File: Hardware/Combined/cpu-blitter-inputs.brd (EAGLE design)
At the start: 177.8 x 152.4 mm, 146 parts, among them IC1 74S08N, IC12 74S08N, IC16 7404N, IC18 7432N, IC20 7430N, IC21 7400N, IC3 74HC573N, IC31 7400N, IC32 7432N, IC4 7404N, IC5 7400N, IC53 7404N, IC54 74LS07N, IC7 74S08N, IC9 74LS74N, J2 TX25-40P-6ST-H1E, U1 W65C02SP, U2 VIA

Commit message: add SMD oscillator to library and fix GRAM power connections
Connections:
- removed net VDD: U$4.32
- removed net VSS: U$4.16
- net GND: now also U$4.16
- net VCC: now also U$4.32
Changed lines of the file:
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@@
 <contactref element="IC3" pad="20"/>
 <contactref element="U$5" pad="28"/>
+<contactref element="U$4" pad="32"/>
 </signal>
 <signal name="GND">
@@
 <contactref element="IC3" pad="1"/>
 <contactref element="U$5" pad="14"/>
+<contactref element="U$4" pad="16"/>
 </signal>
 <signal name="N$1">
@@
 <wire x1="149.86" y1="-17.78" x2="145.0975" y2="-13.0175" width="0.1524" layer="1"/>
 </signal>
-<signal name="VSS">
-<contactref element="U$4" pad="16"/>
-</signal>
-<signal name="VDD">
-<contactref element="U$4" pad="32"/>
-</signal>
 <signal name="AUD_RESET">

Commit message: fix ACP control lines (in schematic)
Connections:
- removed net AUD_SQ1_N: WR_REG_DECODE.15
- removed net AUD_SQ1_X: WR_REG_DECODE.14
- removed net AUD_WAVE_X: WR_REG_DECODE.9
- net !AUD_NMI: now also WR_REG_DECODE.14
- net AUD_RESET: now also WR_REG_DECODE.15
- net AUD_SAMP_RATE_SEL: now also WR_REG_DECODE.9
- net GND: no longer VIAPORT.1
- net VCC: now also VIAPORT.1

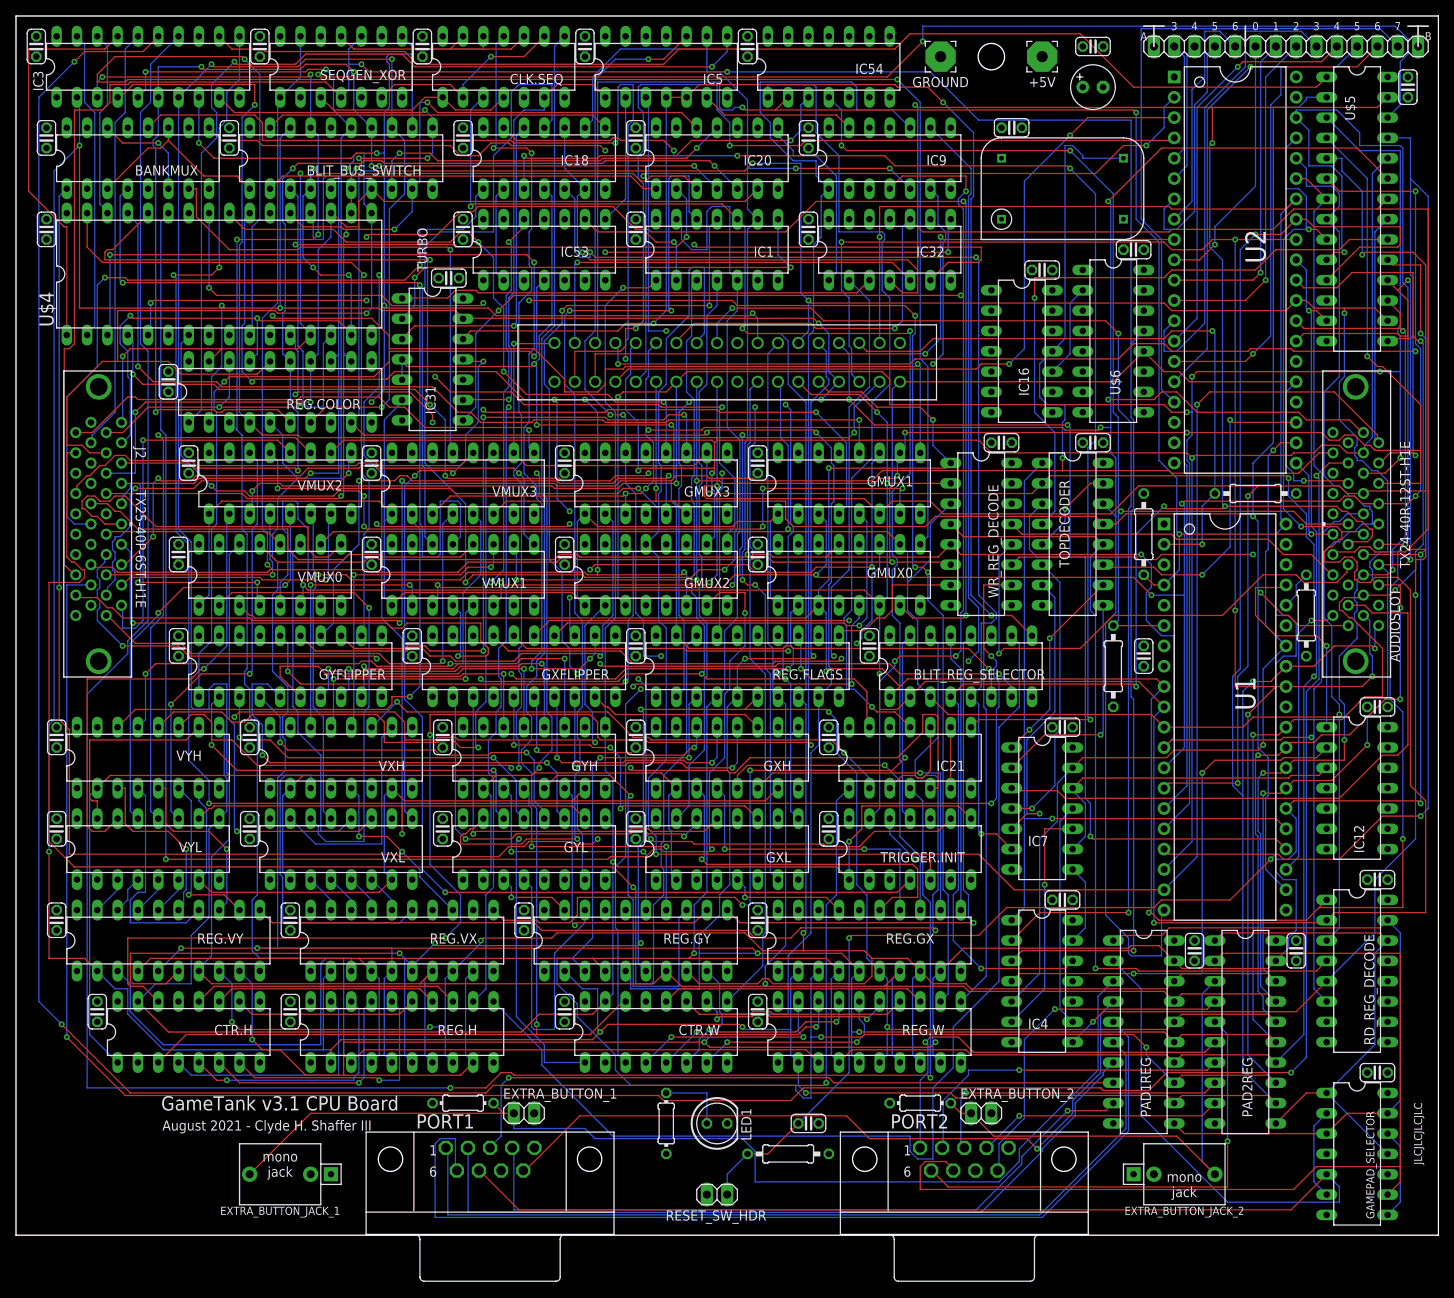
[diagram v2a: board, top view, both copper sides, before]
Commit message: Replace MUX for readregs with spare gates
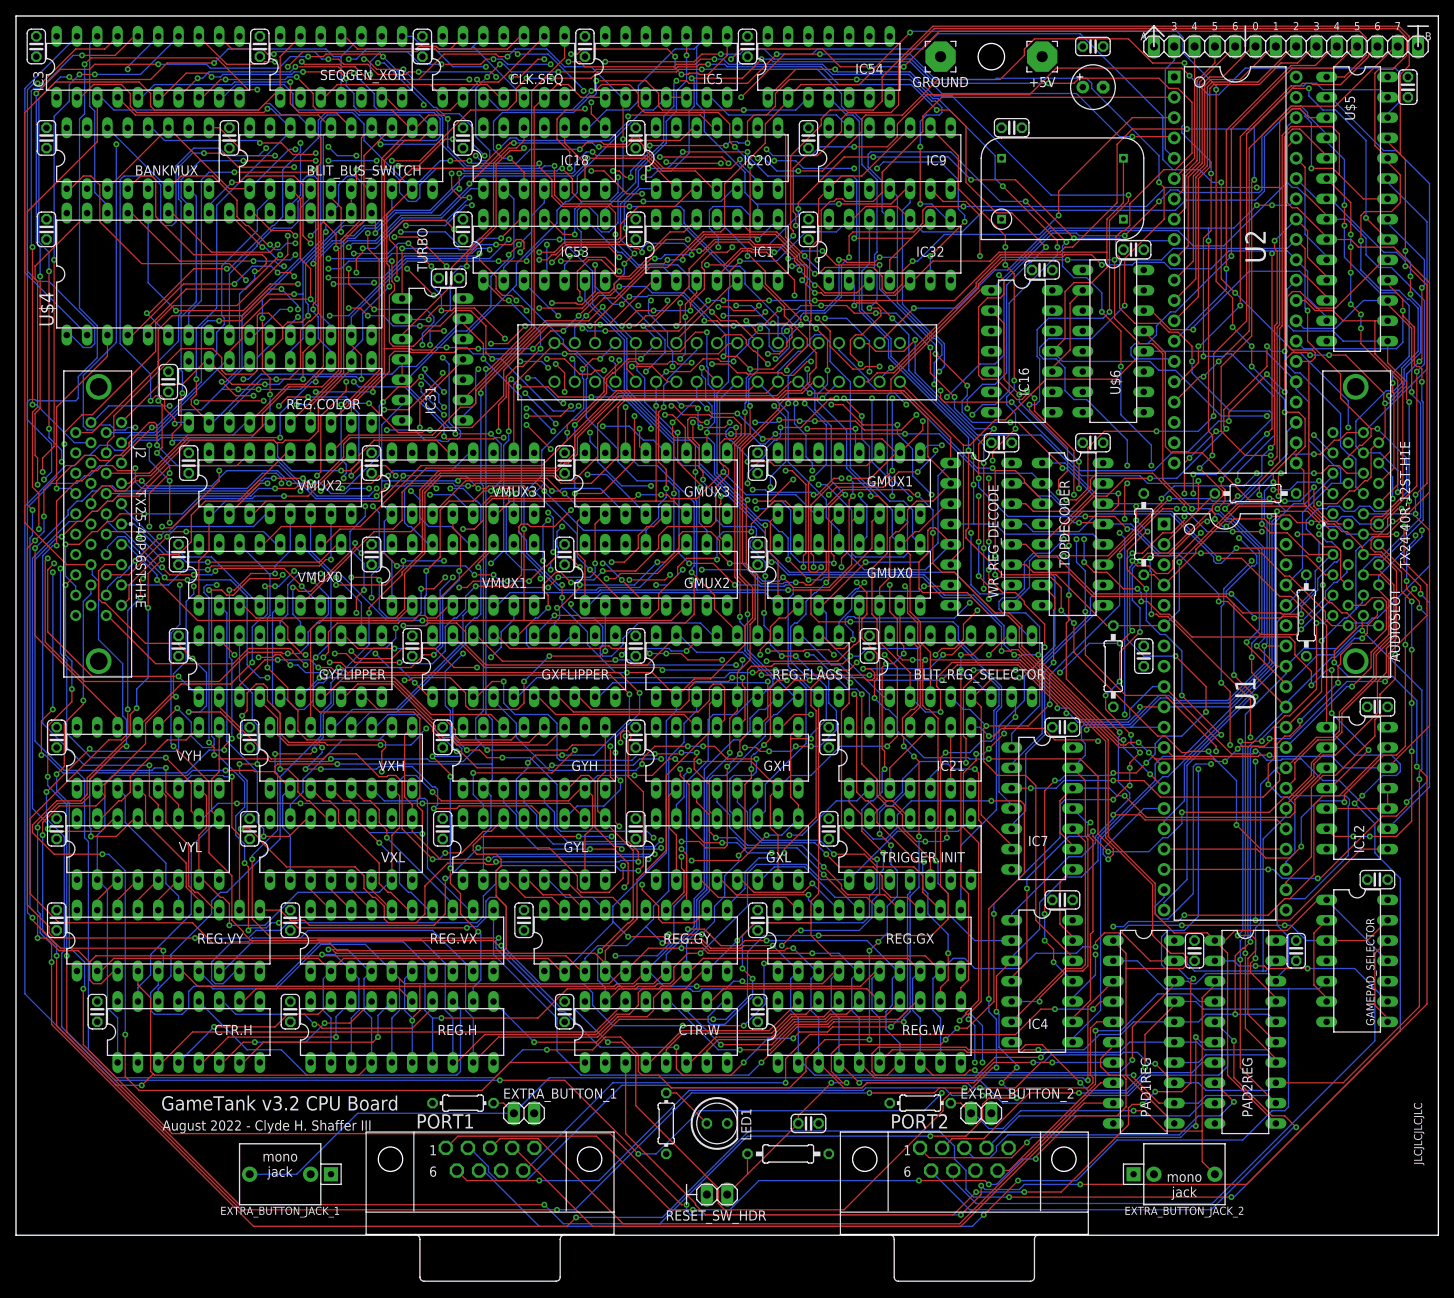
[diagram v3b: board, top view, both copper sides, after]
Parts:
- removed C37: (no value), rcl:C025-024X044
- removed RD_REG_DECODE: 74LS138N, 74xx-us:DIL16
- moved C36 24.1 mm to (170.2, 19.1)
- moved GAMEPAD_SELECTOR 24.1 mm to (167.6, 8.89)
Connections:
- removed net N$91: RD_REG_DECODE.13
- removed net N$92: RD_REG_DECODE.12
- removed net N$93: RD_REG_DECODE.11
- removed net N$95: RD_REG_DECODE.10
- removed net N$97: RD_REG_DECODE.9
- removed net N$99: RD_REG_DECODE.7
- new net N$129: IC12.6, IC53.5
- new net N$149: IC12.13, IC4.10
- new net N$152: IC32.11, IC4.11
- new net N$153: IC12.10, IC12.11, IC12.5
- new net N$154: IC12.4, IC16.2
- new net N$34: IC12.8, IC53.11
- net !GAMEPAD1R: now also IC53.6; no longer RD_REG_DECODE.15
- net !GAMEPAD2R: now also IC53.10; no longer RD_REG_DECODE.14
- net !RE2: now also IC32.13; no longer RD_REG_DECODE.5
- net !REGSSEL: now also IC32.12; no longer RD_REG_DECODE.4
- net A0: now also IC12.9, IC16.1; no longer RD_REG_DECODE.1
- net A1: no longer RD_REG_DECODE.2
- net A2: no longer RD_REG_DECODE.3
- net A3: now also IC12.12; no longer RD_REG_DECODE.6
- net GND: no longer C37.2, RD_REG_DECODE.8
- net VCC: no longer C37.1, RD_REG_DECODE.16
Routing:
- net N$34: track 0.00 -> 248.6 mm, vias 0 -> 16
- net CLK3_5: track 318.9 -> 549.7 mm, vias 4 -> 8
- net N$129: track 0.00 -> 227.2 mm, vias 0 -> 14
- net N$125: track 104.3 -> 293.4 mm, vias 2 -> 15
- net N$152: track 0.00 -> 166.8 mm, vias 0 -> 15
- net N$2: track 157.3 -> 299.4 mm, vias 3 -> 13
- net !GAMEPAD2R: track 63.3 -> 194.3 mm, vias 0 -> 3
- net D0: track 709.6 -> 586.2 mm, vias 13 -> 16
- net N$1: track 88.4 -> 204.0 mm, vias 2 -> 17
- net !GAMEPAD1R: track 89.0 -> 202.6 mm, vias 0 -> 5
- net D2: track 523.2 -> 635.8 mm, vias 6 -> 14
- net OFFSCR_Y: track 114.7 -> 223.5 mm, vias 2 -> 8
- net !RUNNING: track 129.5 -> 237.3 mm, vias 2 -> 14
- net !VID_SEL: track 140.1 -> 242.5 mm, vias 3 -> 14
- net P0: track 143.9 -> 244.6 mm, vias 4 -> 12
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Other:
- board text added: "+5V"
- board text added: "August 2022 - Clyde H. Shaffer III"
- board text added: "GROUND"
- board text added: "GameTank v3.2 CPU Board"
- board text removed: "August 2021 - Clyde H. Shaffer III"
- board text removed: "GameTank v3.1 CPU Board"
